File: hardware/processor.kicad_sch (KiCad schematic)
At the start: 23 parts

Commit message: train schematics
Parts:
- C? (x9): value 100n -> 0.1u; footprint (none) -> Capacitor_SMD:C_0603_1608Metric; Voltage (none) -> 50V
- C? (x5): value 1u -> 4.7u; footprint (none) -> Capacitor_SMD:C_0603_1608Metric; Voltage (none) -> 15V
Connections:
- net 3V3_BACKUP renamed VCC_BKUP_3V3
- net VDD_SYS_EN renamed VDD_AUX_EN
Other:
- company: Erdapfel -> Frisius
- moved on the sheet: AE?, C?, L?

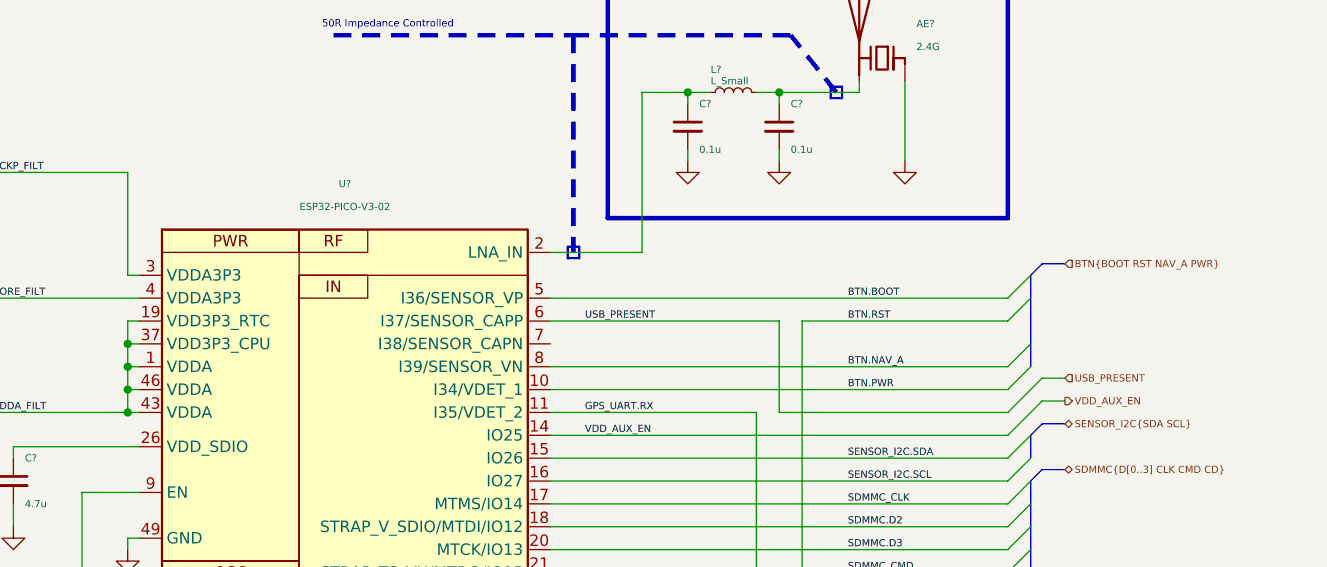
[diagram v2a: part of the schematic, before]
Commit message: usb, bms, proc, btn changes
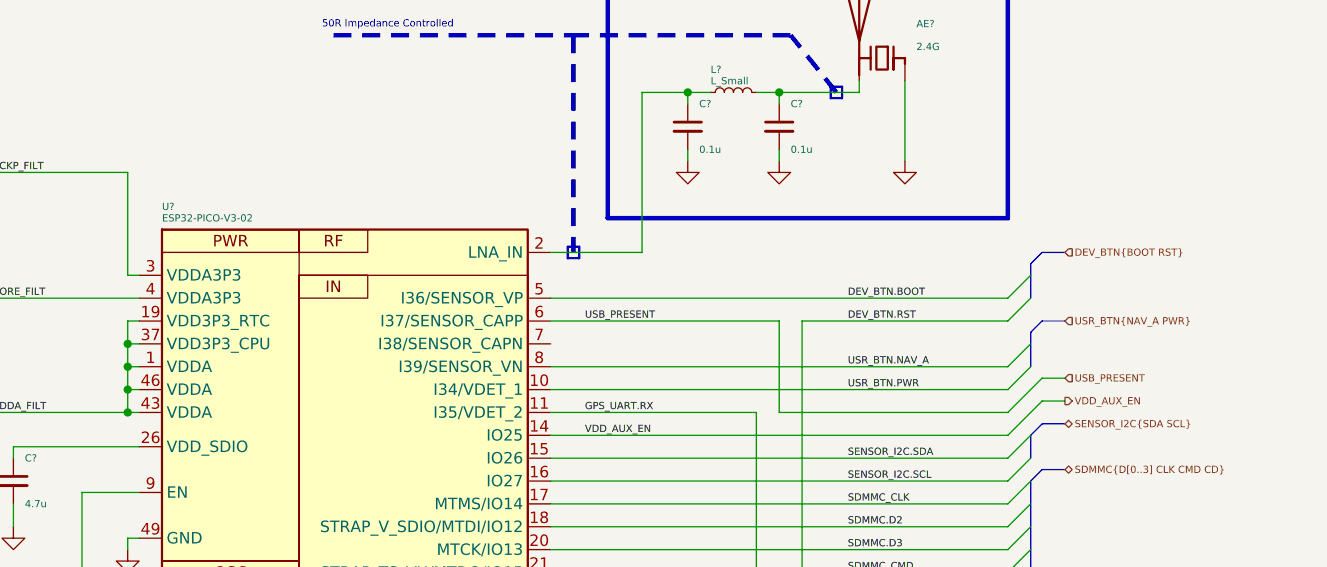
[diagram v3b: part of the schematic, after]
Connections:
- net BTN.BOOT renamed DEV_BTN.BOOT
- net BTN.NAV_A renamed USR_BTN.NAV_A
- net BTN.PWR renamed USR_BTN.PWR
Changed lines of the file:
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@@
+    (stroke (width 0) (type default) (color 0 0 0 0))
+  )
+  (bus_entry (at 217.17 77.47) (size 2.54 -2.54)
     (stroke (width 0) (type default) (color 0 0 0 0))
   )
@@
     (stroke (width 0) (type default) (color 0 0 0 0))
   )
+  (bus_entry (at 217.17 69.85) (size 2.54 -2.54)
+    (stroke (width 0) (type default) (color 0 0 0 0))
+  )
   (bus_entry (at 217.17 72.39) (size 2.54 -2.54)
-    (stroke (width 0) (type default) (color 0 0 0 0))
-  )
-  (bus_entry (at 217.17 69.85) (size 2.54 -2.54)
-    (stroke (width 0) (type default) (color 0 0 0 0))
-  )
-  (bus_entry (at 217.17 77.47) (size 2.54 -2.54)
     (stroke (width 0) (type default) (color 0 0 0 0))
   )
@@
     (stroke (width 0) (type default) (color 0 0 0 0))
   )
-  (bus (pts (xy 219.71 69.85) (xy 219.71 74.93))
-    (stroke (width 0) (type default) (color 0 0 0 0))
-  )
   (wire (pts (xy 114.3 91.44) (xy 120.65 91.44))
     (stroke (width 0) (type default) (color 0 0 0 0))
@@
     (stroke (width 0) (type default) (color 0 0 0 0))
   )
+  (bus (pts (xy 220.98 64.77) (xy 219.71 66.04))
+    (stroke (width 0) (type default) (color 0 0 0 0))
+  )
   (wire (pts (xy 92.71 114.3) (xy 120.65 114.3))
     (stroke (width 0) (type default) (color 0 0 0 0))
@@
   )
   (wire (pts (xy 217.17 85.09) (xy 220.98 81.28))
+    (stroke (width 0) (type default) (color 0 0 0 0))
+  )
+  (bus (pts (xy 219.71 74.93) (xy 219.71 73.66))
     (stroke (width 0) (type default) (color 0 0 0 0))
   )
@@
     (stroke (width 0.25) (type solid) (color 0 0 0 0))
   )
-  (bus (pts (xy 223.52 66.04) (xy 220.98 66.04))
-    (stroke (width 0) (type default) (color 0 0 0 0))
-  )
   (wire (pts (xy 166.37 100.33) (xy 217.17 100.33))
     (stroke (width 0) (type default) (color 0 0 0 0))
   )
   (wire (pts (xy 90.17 77.47) (xy 90.17 76.2))
+    (stroke (width 0) (type default) (color 0 0 0 0))
+  )
+  (bus (pts (xy 219.71 74.93) (xy 219.71 77.47))
     (stroke (width 0) (type default) (color 0 0 0 0))
   )
@@
     (stroke (width 0) (type default) (color 0 0 0 0))
   )
+  (bus (pts (xy 220.98 72.39) (xy 219.71 73.66))
+    (stroke (width 0) (type default) (color 0 0 0 0))
+  )
   (wire (pts (xy 166.37 110.49) (xy 217.17 110.49))
     (stroke (width 0) (type default) (color 0 0 0 0))
@@
     (stroke (width 0) (type default) (color 0 0 0 0))
   )
-  (bus (pts (xy 219.71 74.93) (xy 219.71 77.47))
-    (stroke (width 0) (type default) (color 0 0 0 0))
-  )
   (polyline (pts (xy 168.91 40.64) (xy 168.91 64.77))
     (stroke (width 0.5) (type dot) (color 0 0 0 0))
@@
     (stroke (width 0) (type default) (color 0 0 0 0))
   )
+  (bus (pts (xy 219.71 67.31) (xy 219.71 66.04))
+    (stroke (width 0) (type default) (color 0 0 0 0))
+  )
   (bus (pts (xy 223.52 109.22) (xy 220.98 109.22))
     (stroke (width 0) (type default) (color 0 0 0 0))
@@
     (stroke (width 0) (type default) (color 0 0 0 0))
   )
-  (bus (pts (xy 219.71 67.31) (xy 219.71 69.85))
-    (stroke (width 0) (type default) (color 0 0 0 0))
-  )
   (wire (pts (xy 49.53 54.61) (xy 49.53 55.88))
     (stroke (width 0) (type default) (color 0 0 0 0))
@@
   )
   (wire (pts (xy 166.37 95.25) (xy 217.17 95.25))
+    (stroke (width 0) (type default) (color 0 0 0 0))
+  )
+  (bus (pts (xy 223.52 64.77) (xy 220.98 64.77))
     (stroke (width 0) (type default) (color 0 0 0 0))
   )
@@
     (stroke (width 0) (type default) (color 0 0 0 0))
   )
-  (bus (pts (xy 220.98 66.04) (xy 219.71 67.31))
-    (stroke (width 0) (type default) (color 0 0 0 0))
-  )
   (bus (pts (xy 219.71 135.89) (xy 219.71 133.35))
     (stroke (width 0) (type default) (color 0 0 0 0))
@@
     (stroke (width 0.5) (type dot) (color 0 0 0 0))
   )
+  (bus (pts (xy 223.52 72.39) (xy 220.98 72.39))
+    (stroke (width 0) (type default) (color 0 0 0 0))
+  )
+  (wire (pts (xy 49.53 55.88) (xy 67.31 55.88))
+    (stroke (width 0) (type default) (color 0 0 0 0))
+  )
+  (wire (pts (xy 166.37 80.01) (xy 217.17 80.01))
+    (stroke (width 0) (type default) (color 0 0 0 0))
+  )
+  (wire (pts (xy 90.17 83.82) (xy 90.17 82.55))
+    (stroke (width 0) (type default) (color 0 0 0 0))
+  )
+  (wire (pts (xy 99.06 146.05) (xy 99.06 105.41))
+    (stroke (width 0) (type default) (color 0 0 0 0))
+  )
   (wire (pts (xy 95.25 100.33) (xy 95.25 149.86))
     (stroke (width 0) (type default) (color 0 0 0 0))
   )
-  (wire (pts (xy 49.53 55.88) (xy 67.31 55.88))
-    (stroke (width 0) (type default) (color 0 0 0 0))
-  )
-  (wire (pts (xy 166.37 80.01) (xy 217.17 80.01))
-    (stroke (width 0) (type default) (color 0 0 0 0))
-  )
-  (wire (pts (xy 90.17 83.82) (xy 90.17 82.55))
-    (stroke (width 0) (type default) (color 0 0 0 0))
-  )
-  (wire (pts (xy 99.06 146.05) (xy 99.06 105.41))
-    (stroke (width 0) (type default) (color 0 0 0 0))
-  )
   (wire (pts (xy 49.53 68.58) (xy 49.53 69.85))
     (stroke (width 0) (type default) (color 0 0 0 0))
   )
   (wire (pts (xy 106.68 95.25) (xy 106.68 92.71))
+    (stroke (width 0) (type default) (color 0 0 0 0))
+  )
+  (bus (pts (xy 219.71 67.31) (xy 219.71 69.85))
     (stroke (width 0) (type default) (color 0 0 0 0))
   )
@@
     (effects (font (size 0.8 0.8)) (justify left bottom))
   )
-  (label "BTN.RST" (at 199.39 72.39 0)
+  (label "DEV_BTN.RST" (at 199.39 72.39 0)
     (effects (font (size 0.8 0.8)) (justify left bottom))
   )
@@
     (effects (font (size 0.8 0.8)) (justify left bottom))
   )
-  (label "BTN.PWR" (at 199.39 80.01 0)
+  (label "USR_BTN.PWR" (at 199.39 80.01 0)
     (effects (font (size 0.8 0.8)) (justify left bottom))
   )
@@
     (effects (font (size 0.8 0.8)) (justify left bottom))
   )
-  (label "BTN.BOOT" (at 199.39 69.85 0)
+  (label "DEV_BTN.BOOT" (at 199.39 69.85 0)
     (effects (font (size 0.8 0.8)) (justify left bottom))
   )
@@
     (effects (font (size 0.8 0.8)) (justify left bottom))
   )
-  (label "BTN.NAV_A" (at 199.39 77.47 0)
+  (label "USR_BTN.NAV_A" (at 199.39 77.47 0)
     (effects (font (size 0.8 0.8)) (justify left bottom))
   )
@@
     (effects (font (size 0.8 0.8)) (justify left))
   )
-  (hierarchical_label "BTN{BOOT RST NAV_A PWR}" (shape input) (at 223.52 66.04 0)
+  (hierarchical_label "USR_BTN{NAV_A PWR}" (shape input) (at 223.52 72.39 0)
     (effects (font (size 0.8 0.8)) (justify left))
   )
@@
   )
   (hierarchical_label "DISPLAY{MOSI MISO SCLK CS DC BL}" (shape bidirectional) (at 223.52 109.22 0)
+    (effects (font (size 0.8 0.8)) (justify left))
+  )
+  (hierarchical_label "DEV_BTN{BOOT RST}" (shape input) (at 223.52 64.77 0)
     (effects (font (size 0.8 0.8)) (justify left))
   )
@@
   )
   (symbol (lib_id "bt_MCU_Espressif:ESP32-PICO-V3-02") (at 143.51 99.06 0) (unit 1)
-    (in_bom yes) (on_board yes) (fields_autoplaced)
-    (property "Reference" "U?" (id 0) (at 143.51 57.15 0)
-      (effects (font (size 0.8 0.8)))
-    )
-    (property "Value" "ESP32-PICO-V3-02" (id 1) (at 143.51 59.69 0)
-      (effects (font (size 0.8 0.8)))
+    (in_bom yes) (on_board yes)
+    (property "Reference" "U?" (id 0) (at 123.19 59.69 0)
+      (effects (font (size 0.8 0.8)) (justify left))
+    )
+    (property "Value" "ESP32-PICO-V3-02" (id 1) (at 123.19 60.96 0)
+      (effects (font (size 0.8 0.8)) (justify left))
     )
     (property "Footprint" "Package_DFN_QFN:QFN-48-1EP_7x7mm_P0.5mm_EP5.3x5.3mm" (id 2) (at 143.51 60.96 0)

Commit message: started b2b and power
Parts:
- added R?: 10k, symbol Device:R_Small
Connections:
- net BTN.RST: now also R?.2
- net VCC_BKUP_3V3: now also R?.1
- net CHARGE_STAT: now reaches U?.7 (I38/SENSOR_CAPN)

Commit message: checking footprint assignment, added current sense pac1934 for dev
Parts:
- AE1: renamed from AE?; footprint (none) -> RF_Antenna:Texas_SWRA117D_2.4GHz_Left
- C3, C4: renamed from C?; footprint (none) -> Capacitor_SMD:C_0603_1608Metric
- L1, L2, L3: renamed from L?; footprint (none) -> Inductor_SMD:L_0603_1608Metric
- L4: renamed from L?; footprint (none) -> Inductor_SMD:L_0402_1005Metric
- R1, R2: renamed from R?; footprint (none) -> Resistor_SMD:R_0603_1608Metric
- gave numbers to parts that had none: 15

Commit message: hardware update
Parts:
- removed C10, C11, C12, C13: 4.7u, Capacitor_SMD:C_0603_1608Metric, symbol Device:C_Small
- removed C3: DNF, Capacitor_SMD:C_0603_1608Metric, symbol Device:C_Small
- removed C6, C9: 0.1u, Capacitor_SMD:C_0603_1608Metric, symbol Device:C_Small
- removed L2, L3: 0R, Inductor_SMD:L_0603_1608Metric, symbol Device:L_Small
- removed R2: 10k, Resistor_SMD:R_0603_1608Metric, symbol Device:R_Small
- added C2: 1u, Capacitor_SMD:C_0603_1608Metric, symbol Device:C_Small
- C1: value 0.1u -> 1u
- C10: renamed from C16; footprint Capacitor_SMD:C_0603_1608Metric -> Capacitor_SMD:C_0402_1005Metric
- C3: renamed from C2; footprint Capacitor_SMD:C_0603_1608Metric -> Capacitor_SMD:C_0402_1005Metric
- C4: value DNF -> 1u; Voltage (none) -> 50V
- C5: renamed from C8; footprint Capacitor_SMD:C_0603_1608Metric -> Capacitor_SMD:C_0402_1005Metric
- C6: renamed from C5; footprint Capacitor_SMD:C_0603_1608Metric -> Capacitor_SMD:C_0402_1005Metric
- C7: footprint Capacitor_SMD:C_0603_1608Metric -> Capacitor_SMD:C_0402_1005Metric
- C8: renamed from C14; value 4.7u -> 1u
- C9: renamed from C15; footprint Capacitor_SMD:C_0603_1608Metric -> Capacitor_SMD:C_0402_1005Metric
- L1: value L_Small -> 0; footprint Inductor_SMD:L_0603_1608Metric -> Resistor_SMD:R_0603_1608Metric
- R1: value 10k -> 100k; footprint Resistor_SMD:R_0603_1608Metric -> Resistor_SMD:R_0402_1005Metric
- renumbered L4 to L2, U3 to U1
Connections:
- net 3V3_CORE: now also C5.1, C7.1, U1.19 (VDD3P3_RTC), U1.37 (VDD3P3_CPU), C2.1
- net 3V3_ESP_VDDA_FILT: now also U1.3 (VDDA3P3), U1.4 (VDDA3P3); no longer U1.19 (VDD3P3_RTC), U1.37 (VDD3P3_CPU)
- net GND: now also AE1.2 (PCB_Trace), C2.2; no longer AE1.1 (FEED)
- net at C10.1, L2.2: now also AE1.1 (FEED); no longer AE1.2 (PCB_Trace)
- removed net 3V3_ESP_BCKP_FILT: C7.1, U1.3 (VDDA3P3)
- removed net 3V3_ESP_CORE_FILT: C5.1, U1.4 (VDDA3P3)
- net CHARGE_STAT: no longer names the net of U1.7 (I38/SENSOR_CAPN)
- net VDD_CORE_EN renamed 3V3_CORE_EN
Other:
- moved on the sheet: AE1, C1, C3, C5, C6, C7, C8, L1

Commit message: initial component placement and design simplification
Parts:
- L1: footprint Resistor_SMD:R_0603_1608Metric -> Resistor_SMD:R_0402_1005Metric
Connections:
- net SDMMC_CD renamed SDMMC.CD
- net SDMMC_CLK renamed SDMMC.CLK
- net SDMMC_CMD renamed SDMMC.CMD
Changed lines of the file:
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@@
     (effects (font (size 0.8 0.8)) (justify left bottom))
   )
-  (label "SDMMC_CD" (at 199.39 105.41 0)
+  (label "SDMMC.CD" (at 199.39 105.41 0)
     (effects (font (size 0.8 0.8)) (justify left bottom))
   )
@@
     (effects (font (size 0.8 0.8)) (justify left bottom))
   )
-  (label "SDMMC_CLK" (at 199.39 92.71 0)
+  (label "SDMMC.CLK" (at 199.39 92.71 0)
     (effects (font (size 0.8 0.8)) (justify left bottom))
   )
@@
     (effects (font (size 0.8 0.8)) (justify left bottom))
   )
-  (label "SDMMC_CMD" (at 199.39 100.33 0)
+  (label "SDMMC.CMD" (at 199.39 100.33 0)
     (effects (font (size 0.8 0.8)) (justify left bottom))
   )
@@
     (effects (font (size 0.8 0.8)) (justify left bottom))
   )
-  (hierarchical_label "GPS_UART{RXD TXD}" (shape bidirectional) (at 223.52 129.54 0)
+  (hierarchical_label "GPS_UART{RX TX}" (shape bidirectional) (at 223.52 129.54 0)
     (effects (font (size 0.8 0.8)) (justify left))
   )
@@
       (effects (font (size 0.8 0.8)))
     )
-    (property "Footprint" "Resistor_SMD:R_0603_1608Metric" (id 2) (at 81.28 82.55 0)
-      (effects (font (size 0.8 0.8)) hide)
-    )
+    (property "Footprint" "Resistor_SMD:R_0402_1005Metric" (id 2) (at 81.28 82.55 0)
+      (effects (font (size 0.8 0.8)) hide)
+    )

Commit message: fixing submodule
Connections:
- net SPARE0: now reaches U1.7 (I38/SENSOR_CAPN)
- net 3V3_CORE_EN renamed POWER_EN
- net SDMMC.CD renamed SPARE2
- net VDD_AUX_EN renamed SPARE1
